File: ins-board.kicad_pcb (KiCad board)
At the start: 4 copper layers, 50 x 23 mm, 94 parts, among them P1 PWR, P2 Power (Solder Pad), Q1 FDN306P, Q2 FDC638APZ, U1 24LC128, U10 HMC5883L, U11 H3LIS331DL, U2 STM32F415RGT6, U3 LTC4412, U4 MAX3051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

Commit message: optimize routing
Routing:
- net GND: track 140.3 -> 142.7 mm, vias 25 -> 26
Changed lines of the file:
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@@
     (thickness 1.6)
     (drawings 13)
-    (tracks 1273)
+    (tracks 1281)
     (zones 0)
     (modules 94)
@@
   (segment (start 45.6646 38.5646) (end 45.6646 38.3872) (width 0.2032) (layer F.Cu) (net 28))
   (segment (start 45.6646 38.3872) (end 45.6646 38.5646) (width 0.2032) (layer F.Cu) (net 28))
-  (segment (start 44.4146 38.3872) (end 44.4146 38.7554) (width 0.2032) (layer F.Cu) (net 29) (status C00000))
-  (segment (start 43.4132 38.4868) (end 44.2698 38.4868) (width 0.2032) (layer B.Cu) (net 29) (status 800000))
+  (segment (start 44.4146 38.3872) (end 44.4146 38.7554) (width 0.2032) (layer F.Cu) (net 29))
+  (segment (start 43.4132 38.4868) (end 44.2698 38.4868) (width 0.2032) (layer B.Cu) (net 29))
   (segment (start 42.38 39.52) (end 43.4132 38.4868) (width 0.2032) (layer B.Cu) (net 29))
   (via (at 42.38 39.52) (size 0.706) (layers F.Cu B.Cu) (net 29))
   (segment (start 42.43 39.47) (end 42.38 39.52) (width 0.2032) (layer F.Cu) (net 29))
   (segment (start 43.7 39.47) (end 42.43 39.47) (width 0.2032) (layer F.Cu) (net 29))
-  (segment (start 44.4146 38.7554) (end 43.7 39.47) (width 0.2032) (layer F.Cu) (net 29) (status 400000))
+  (segment (start 44.4146 38.7554) (end 43.7 39.47) (width 0.2032) (layer F.Cu) (net 29))
   (segment (start 46.6 41.9) (end 46.6 42.05) (width 0.2032) (layer B.Cu) (net 29))
   (segment (start 46.6 42.05) (end 45.7 42.95) (width 0.2032) (layer B.Cu) (net 29))
@@
   (segment (start 61.4 44.4) (end 59.8 46) (width 0.2032) (layer F.Cu) (net 35))
   (segment (start 48.5 45.5) (end 49.275 45.5) (width 0.2032) (layer F.Cu) (net 35))
-  (segment (start 46.95 44.05) (end 47.04 44.05) (width 0.254) (layer F.Cu) (net 36) (status C00000))
+  (segment (start 46.95 44.05) (end 47.04 44.05) (width 0.254) (layer F.Cu) (net 36))
   (segment (start 47.62 42.23) (end 48.5 41.35) (width 0.254) (layer F.Cu) (net 36))
   (segment (start 47.62 43.47) (end 47.62 42.23) (width 0.254) (layer F.Cu) (net 36))
-  (segment (start 47.04 44.05) (end 47.62 43.47) (width 0.254) (layer F.Cu) (net 36) (status 400000))
+  (segment (start 47.04 44.05) (end 47.62 43.47) (width 0.254) (layer F.Cu) (net 36))
   (segment (start 46.75 34.2) (end 46.75 35.05) (width 0.2032) (layer F.Cu) (net 36))
   (segment (start 46.75 35.05) (end 48 36.3) (width 0.2032) (layer F.Cu) (net 36))
@@
   (segment (start 66.25 38.75) (end 66 39) (width 0.2032) (layer F.Cu) (net 51))
   (segment (start 66.25 38.75) (end 66 39) (width 0.2032) (layer F.Cu) (net 51))
+  (segment (start 39.925 36.375) (end 39.925 37.325) (width 0.254) (layer F.Cu) (net 52) (status 400000))
+  (segment (start 39.9288 37.9988) (end 39.9288 38.4868) (width 0.254) (layer B.Cu) (net 52) (status 800000))
+  (segment (start 39.59 37.66) (end 39.9288 37.9988) (width 0.254) (layer B.Cu) (net 52))
+  (via (at 39.59 37.66) (size 0.706) (layers F.Cu B.Cu) (net 52))
+  (segment (start 39.925 37.325) (end 39.59 37.66) (width 0.254) (layer F.Cu) (net 52))
   (segment (start 49.99 42.08) (end 49.99 41.91) (width 0.254) (layer F.Cu) (net 52))
-  (segment (start 49.99 41.91) (end 50.65 41.25) (width 0.254) (layer F.Cu) (net 52) (status 800000))
-  (segment (start 47.9 43.65) (end 47.9 43.5) (width 0.254) (layer B.Cu) (net 52) (status C00000))
+  (segment (start 49.99 41.91) (end 50.65 41.25) (width 0.254) (layer F.Cu) (net 52))
+  (segment (start 47.9 43.65) (end 47.9 43.5) (width 0.254) (layer B.Cu) (net 52))
   (segment (start 48.91 42.08) (end 49.99 42.08) (width 0.254) (layer F.Cu) (net 52))
   (segment (start 49.99 42.08) (end 50 42.08) (width 0.254) (layer F.Cu) (net 52))
@@
   (segment (start 48.32 43.08) (end 48.32 42.67) (width 0.254) (layer F.Cu) (net 52))
   (via (at 48.32 43.08) (size 0.706) (layers F.Cu B.Cu) (net 52))
-  (segment (start 47.9 43.5) (end 48.32 43.08) (width 0.254) (layer B.Cu) (net 52) (status 400000))
+  (segment (start 47.9 43.5) (end 48.32 43.08) (width 0.254) (layer B.Cu) (net 52))
   (segment (start 57.225 37.25) (end 55.78 37.25) (width 0.2032) (layer B.Cu) (net 52))
   (segment (start 55.6 37.07) (end 55.6 36.25) (width 0.2032) (layer B.Cu) (net 52))
@@
   (via (at 54.6 44.35) (size 0.706) (layers F.Cu B.Cu) (net 76))
   (segment (start 54.45 44.5) (end 54.6 44.35) (width 0.2032) (layer F.Cu) (net 76))
-  (segment (start 41.45 39.8) (end 41.45 33) (width 0.2032) (layer Inner2.Cu) (net 77))
-  (segment (start 41.45 33) (end 42.01 32.44) (width 0.2032) (layer Inner2.Cu) (net 77))
+  (segment (start 41.45 39.8) (end 41.45 39.25) (width 0.2032) (layer Inner2.Cu) (net 77))
+  (segment (start 42.55 38.15) (end 42.55 31.9) (width 0.2032) (layer Inner2.Cu) (net 77))
+  (segment (start 41.45 39.25) (end 42.55 38.15) (width 0.2032) (layer Inner2.Cu) (net 77))
+  (segment (start 40.73 37.75) (end 40.71 37.75) (width 0.2032) (layer B.Cu) (net 77))
+  (segment (start 39.71 36.75) (end 39 36.75) (width 0.2032) (layer B.Cu) (net 77))
+  (segment (start 40.71 37.75) (end 39.71 36.75) (width 0.2032) (layer B.Cu) (net 77))
   (segment (start 52.4 30.7) (end 53.75 30.7) (width 0.2032) (layer B.Cu) (net 77))
   (segment (start 53.75 30.7) (end 54.4 30.7) (width 0.254) (layer B.Cu) (net 77))
@@
   (via (at 41.45 39.8) (size 0.706) (layers F.Cu B.Cu) (net 77))
   (segment (start 39 36.75) (end 38.1 36.75) (width 0.2032) (layer B.Cu) (net 77))
-  (segment (start 40 37.75) (end 39 36.75) (width 0.2032) (layer B.Cu) (net 77))
-  (segment (start 40.95 37.75) (end 40 37.75) (width 0.2032) (layer B.Cu) (net 77))
+  (segment (start 40.95 37.75) (end 40.73 37.75) (width 0.2032) (layer B.Cu) (net 77))
   (segment (start 41.45 38.25) (end 40.95 37.75) (width 0.2032) (layer B.Cu) (net 77))
   (segment (start 74.25 35.9) (end 75.1 35.9) (width 0.254) (layer F.Cu) (net 77))
@@
   (segment (start 53.4 29.5) (end 54.05 28.85) (width 0.2032) (layer Inner2.Cu) (net 77))
   (segment (start 44.95 29.5) (end 53.4 29.5) (width 0.2032) (layer Inner2.Cu) (net 77))
-  (segment (start 42.01 32.44) (end 44.95 29.5) (width 0.2032) (layer Inner2.Cu) (net 77))
+  (segment (start 42.55 31.9) (end 44.95 29.5) (width 0.2032) (layer Inner2.Cu) (net 77))
   (segment (start 52.8828 28.1328) (end 54.3276 28.1328) (width 0.3556) (layer B.Cu) (net 77))
   (segment (start 54.3276 28.1328) (end 54.7116 27.7488) (width 0.3556) (layer B.Cu) (net 77))

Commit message: optimize zones
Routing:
- net GND: track 142.7 -> 143.3 mm
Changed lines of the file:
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@@
     (thickness 1.6)
     (drawings 13)
-    (tracks 1281)
+    (tracks 1282)
     (zones 0)
     (modules 94)
@@
     (22 B.Mask user)
     (23 F.Mask user)
-    (24 Dwgs.User user)
+    (24 Dwgs.User user hide)
     (25 Cmts.User user hide)
     (26 Eco1.User user)
@@
   (segment (start 66.25 38.75) (end 66 39) (width 0.2032) (layer F.Cu) (net 51))
   (segment (start 66.25 38.75) (end 66 39) (width 0.2032) (layer F.Cu) (net 51))
-  (segment (start 39.925 36.375) (end 39.925 37.325) (width 0.254) (layer F.Cu) (net 52) (status 400000))
-  (segment (start 39.9288 37.9988) (end 39.9288 38.4868) (width 0.254) (layer B.Cu) (net 52) (status 800000))
+  (segment (start 79 43.25) (end 79.65 43.25) (width 0.508) (layer Inner2.Cu) (net 52))
+  (segment (start 46.15 31.9) (end 47.6 31.9) (width 0.2032) (layer F.Cu) (net 52))
+  (via (at 48 32.3) (size 0.706) (layers F.Cu B.Cu) (net 52))
+  (segment (start 47.6 31.9) (end 48 32.3) (width 0.2032) (layer F.Cu) (net 52))
+  (segment (start 39.925 36.375) (end 39.925 37.325) (width 0.254) (layer F.Cu) (net 52))
+  (segment (start 39.9288 37.9988) (end 39.9288 38.4868) (width 0.254) (layer B.Cu) (net 52))
   (segment (start 39.59 37.66) (end 39.9288 37.9988) (width 0.254) (layer B.Cu) (net 52))
   (via (at 39.59 37.66) (size 0.706) (layers F.Cu B.Cu) (net 52))
@@
   (segment (start 44.1 43.55) (end 44.1 43.2) (width 0.2032) (layer F.Cu) (net 52))
   (via (at 44.1 43.2) (size 0.706) (layers F.Cu B.Cu) (net 52))
-  (segment (start 46.15 31.9) (end 47.6 31.9) (width 0.2032) (layer F.Cu) (net 52))
-  (via (at 48 32.3) (size 0.706) (layers F.Cu B.Cu) (net 52))
-  (segment (start 47.6 31.9) (end 48 32.3) (width 0.2032) (layer F.Cu) (net 52))
   (segment (start 57.35 27.5) (end 56.75 26.9) (width 0.3048) (layer B.Cu) (net 52))
   (segment (start 56.75 26.9) (end 56 26.9) (width 0.3048) (layer B.Cu) (net 52))
@@
   (via (at 54.6 44.35) (size 0.706) (layers F.Cu B.Cu) (net 76))
   (segment (start 54.45 44.5) (end 54.6 44.35) (width 0.2032) (layer F.Cu) (net 76))
+  (segment (start 44.275 30.175) (end 45.6 28.85) (width 0.2032) (layer Inner2.Cu) (net 77))
+  (segment (start 45.6 28.85) (end 54.05 28.85) (width 0.2032) (layer Inner2.Cu) (net 77))
   (segment (start 41.45 39.8) (end 41.45 39.25) (width 0.2032) (layer Inner2.Cu) (net 77))
   (segment (start 42.55 38.15) (end 42.55 31.9) (width 0.2032) (layer Inner2.Cu) (net 77))
@@
   (segment (start 54.95 28.85) (end 56.05 29.95) (width 0.2032) (layer Inner2.Cu) (net 77))
   (segment (start 54.05 28.85) (end 54.95 28.85) (width 0.2032) (layer Inner2.Cu) (net 77))
-  (segment (start 53.4 29.5) (end 54.05 28.85) (width 0.2032) (layer Inner2.Cu) (net 77))
-  (segment (start 44.95 29.5) (end 53.4 29.5) (width 0.2032) (layer Inner2.Cu) (net 77))
-  (segment (start 42.55 31.9) (end 44.95 29.5) (width 0.2032) (layer Inner2.Cu) (net 77))
+  (segment (start 42.55 31.9) (end 44.275 30.175) (width 0.2032) (layer Inner2.Cu) (net 77))
   (segment (start 52.8828 28.1328) (end 54.3276 28.1328) (width 0.3556) (layer B.Cu) (net 77))
   (segment (start 54.3276 28.1328) (end 54.7116 27.7488) (width 0.3556) (layer B.Cu) (net 77))
@@
     (polygon
       (pts
-        (xy 55 47.8) (xy 43 47.8) (xy 43 33) (xy 55 33)
+        (xy 55 47.8) (xy 43 47.8) (xy 42.99 32.68) (xy 44.68 30.95) (xy 49.1 30.98)
+        (xy 51.14 33.01) (xy 55 33)
       )
     )
@@
     (polygon
       (pts
-        (xy 55.8 47.8) (xy 79 47.8) (xy 79 27.2) (xy 52 27.2) (xy 52 32.4)
-        (xy 55.8 32.4)
+        (xy 55.8 48.7) (xy 78.9 48.7) (xy 78.9 33.25) (xy 77.3 31.65) (xy 72.4 31.5)
+        (xy 68.7 27.95) (xy 45.78 27.9) (xy 44.42 29.27) (xy 44.42 30.62) (xy 49.29 30.63)
+        (xy 51.1 32.4) (xy 55.8 32.4)
       )
     )
@@
     (polygon
       (pts
-        (xy 32.3 26.3) (xy 51.3 26.3) (xy 51.3 32.4) (xy 42.5 32.4) (xy 42.5 48.7)
-        (xy 32.3 48.7)
+        (xy 81.7 48.7) (xy 79.35 48.7) (xy 79.35 32.7) (xy 77.5 31.1) (xy 72.55 31.1)
+        (xy 68.9 27.5) (xy 62.45 27.5) (xy 62.05 26.92) (xy 45.75 26.9) (xy 44.11 28.64)
+        (xy 44.09 30.92) (xy 42.49 32.66) (xy 42.5 48.7) (xy 32.3 48.7) (xy 32.3 26.3)
+        (xy 81.7 26.3)
       )
     )

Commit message: optimize routing
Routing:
- net GND: track 143.3 -> 144.7 mm
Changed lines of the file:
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@@
     (thickness 1.6)
     (drawings 13)
-    (tracks 1282)
+    (tracks 1293)
     (zones 0)
     (modules 94)
@@
   )
   (setup
-    (last_trace_width 0.2032)
+    (last_trace_width 0.254)
     (user_trace_width 0.1524)
     (user_trace_width 0.2032)
@@
   (segment (start 61.05 43.85) (end 56.15 43.85) (width 0.2032) (layer B.Cu) (net 27))
   (segment (start 62.2 42.7) (end 61.05 43.85) (width 0.2032) (layer B.Cu) (net 27))
-  (segment (start 45.6646 38.3872) (end 45.6646 38.9646) (width 0.2032) (layer F.Cu) (net 28))
-  (segment (start 45.6646 38.9646) (end 46.2 39.5) (width 0.2032) (layer F.Cu) (net 28))
+  (segment (start 45.6646 38.3872) (end 45.8 38.5226) (width 0.2032) (layer F.Cu) (net 28))
+  (segment (start 45.8 38.5226) (end 45.8 39.1) (width 0.2032) (layer F.Cu) (net 28))
+  (segment (start 45.8 39.1) (end 46.2 39.5) (width 0.2032) (layer F.Cu) (net 28))
   (segment (start 46.85 39.75) (end 46.45 39.75) (width 0.2032) (layer F.Cu) (net 28))
   (segment (start 46.45 39.75) (end 46.2 39.5) (width 0.2032) (layer F.Cu) (net 28))
@@
   (segment (start 66.25 38.75) (end 66 39) (width 0.2032) (layer F.Cu) (net 51))
   (segment (start 66.25 38.75) (end 66 39) (width 0.2032) (layer F.Cu) (net 51))
+  (segment (start 60.6 33) (end 60.45 33.15) (width 0.254) (layer F.Cu) (net 52))
+  (segment (start 59.5 33.15) (end 59.2 33.45) (width 0.254) (layer F.Cu) (net 52) (status C00000))
+  (segment (start 59.7 33.15) (end 59.5 33.15) (width 0.254) (layer F.Cu) (net 52) (status C00000))
+  (segment (start 60.45 33.15) (end 59.7 33.15) (width 0.254) (layer F.Cu) (net 52) (status 800000))
+  (segment (start 60.6 32.45) (end 60.25 32.8) (width 0.254) (layer F.Cu) (net 52) (status 400000))
+  (segment (start 60.25 32.8) (end 60.25 33) (width 0.254) (layer F.Cu) (net 52))
+  (segment (start 60.25 33) (end 60.6 33) (width 0.254) (layer F.Cu) (net 52))
+  (segment (start 50.65 41.25) (end 50.65 41.42) (width 0.254) (layer F.Cu) (net 52) (status C00000))
+  (segment (start 50.65 41.42) (end 49.99 42.08) (width 0.254) (layer F.Cu) (net 52) (status 400000))
+  (segment (start 43.2428 40.386) (end 43.2428 40.6072) (width 0.254) (layer F.Cu) (net 52))
+  (segment (start 42.6 41.25) (end 42.4 41.25) (width 0.254) (layer F.Cu) (net 52))
+  (segment (start 43.2428 40.6072) (end 42.6 41.25) (width 0.254) (layer F.Cu) (net 52))
+  (segment (start 43.5984 34.544) (end 43.5984 34.8016) (width 0.254) (layer F.Cu) (net 52))
+  (segment (start 43.5984 34.8016) (end 43.1646 35.2354) (width 0.254) (layer F.Cu) (net 52))
   (segment (start 79 43.25) (end 79.65 43.25) (width 0.508) (layer Inner2.Cu) (net 52))
   (segment (start 46.15 31.9) (end 47.6 31.9) (width 0.2032) (layer F.Cu) (net 52))
@@
   (via (at 39.59 37.66) (size 0.706) (layers F.Cu B.Cu) (net 52))
   (segment (start 39.925 37.325) (end 39.59 37.66) (width 0.254) (layer F.Cu) (net 52))
-  (segment (start 49.99 42.08) (end 49.99 41.91) (width 0.254) (layer F.Cu) (net 52))
-  (segment (start 49.99 41.91) (end 50.65 41.25) (width 0.254) (layer F.Cu) (net 52))
   (segment (start 47.9 43.65) (end 47.9 43.5) (width 0.254) (layer B.Cu) (net 52))
   (segment (start 48.91 42.08) (end 49.99 42.08) (width 0.254) (layer F.Cu) (net 52))
@@
   (segment (start 50 42.75) (end 50 42.08) (width 0.2032) (layer F.Cu) (net 52))
   (segment (start 47.9 39.55) (end 49.4 39.55) (width 0.254) (layer B.Cu) (net 52))
-  (segment (start 43.2428 40.386) (end 43.2428 40.4072) (width 0.254) (layer F.Cu) (net 52))
-  (segment (start 43.2428 40.4072) (end 42.4 41.25) (width 0.254) (layer F.Cu) (net 52))
   (segment (start 42.4 41.25) (end 42.65 41.25) (width 0.2032) (layer B.Cu) (net 52))
   (via (at 42.4 41.25) (size 0.706) (layers F.Cu B.Cu) (net 52))
@@
   (segment (start 42.95 40.3) (end 43.4632 39.7868) (width 0.254) (layer B.Cu) (net 52))
   (segment (start 41.9146 38.3872) (end 41.9146 36.1872) (width 0.254) (layer F.Cu) (net 52))
-  (segment (start 43.1646 36.1872) (end 43.1646 34.9778) (width 0.254) (layer F.Cu) (net 52))
-  (segment (start 43.1646 34.9778) (end 43.5984 34.544) (width 0.254) (layer F.Cu) (net 52))
+  (segment (start 43.1646 36.1872) (end 43.1646 35.2354) (width 0.254) (layer F.Cu) (net 52))
   (segment (start 66.7 41.975) (end 66.7 40.65) (width 0.2032) (layer B.Cu) (net 52))
   (via (at 66.7 40.65) (size 0.706) (layers F.Cu B.Cu) (net 52))
@@
   (via (at 55.1 40.8) (size 0.706) (layers F.Cu B.Cu) (net 52))
   (segment (start 61 30.4) (end 61 32.6) (width 0.254) (layer B.Cu) (net 52))
+  (segment (start 61 32.6) (end 60.6 33) (width 0.254) (layer B.Cu) (net 52))
   (via (at 60.6 33) (size 0.706) (layers F.Cu B.Cu) (net 52))
   (segment (start 60.6 33) (end 60.6 32.45) (width 0.254) (layer F.Cu) (net 52))
-  (segment (start 61 32.6) (end 60.6 33) (width 0.254) (layer B.Cu) (net 52))
   (segment (start 66.25 45.2) (end 67.6 45.2) (width 0.254) (layer B.Cu) (net 52))
   (segment (start 67.6 45.2) (end 67.7 45.1) (width 0.254) (layer B.Cu) (net 52))
@@
   (segment (start 61.6 32.6) (end 61.45 32.45) (width 0.254) (layer F.Cu) (net 52))
   (segment (start 61.45 32.45) (end 60.2 32.45) (width 0.254) (layer F.Cu) (net 52))
-  (segment (start 60.2 32.45) (end 59.2 33.45) (width 0.3048) (layer F.Cu) (net 52))
   (segment (start 77.35 31.125) (end 78.375 31.125) (width 0.3048) (layer F.Cu) (net 52))
   (segment (start 78.375 32.375) (end 77.35 32.375) (width 0.3048) (layer B.Cu) (net 52))
@@
   (via (at 54.6 44.35) (size 0.706) (layers F.Cu B.Cu) (net 76))
   (segment (start 54.45 44.5) (end 54.6 44.35) (width 0.2032) (layer F.Cu) (net 76))
+  (segment (start 70.35 31.65) (end 70.45 31.65) (width 0.2032) (layer F.Cu) (net 77) (status C00000))
+  (segment (start 70.95 32.15) (end 70.95 32.35) (width 0.2032) (layer F.Cu) (net 77))
+  (segment (start 70.45 31.65) (end 70.95 32.15) (width 0.2032) (layer F.Cu) (net 77) (status 400000))
   (segment (start 44.275 30.175) (end 45.6 28.85) (width 0.2032) (layer Inner2.Cu) (net 77))
   (segment (start 45.6 28.85) (end 54.05 28.85) (width 0.2032) (layer Inner2.Cu) (net 77))
@@
   (segment (start 63.44 46.99) (end 63.8 47.35) (width 0.254) (layer F.Cu) (net 77))
   (segment (start 63.1324 46.99) (end 63.44 46.99) (width 0.254) (layer F.Cu) (net 77))
-  (segment (start 70.35 31.65) (end 70.35 31.75) (width 0.2032) (layer F.Cu) (net 77))
   (segment (start 72.45 32.7) (end 73.3 31.85) (width 0.2032) (layer F.Cu) (net 77))
   (segment (start 71.3 32.7) (end 72.45 32.7) (width 0.2032) (layer F.Cu) (net 77))
-  (segment (start 70.35 31.75) (end 71.3 32.7) (width 0.2032) (layer F.Cu) (net 77))
+  (segment (start 70.95 32.35) (end 71.3 32.7) (width 0.2032) (layer F.Cu) (net 77))
   (segment (start 69.25 45.5) (end 69.65 45.5) (width 0.254) (layer F.Cu) (net 77))
   (segment (start 69.7 45.5) (end 70.5 46.3) (width 0.254) (layer F.Cu) (net 77))

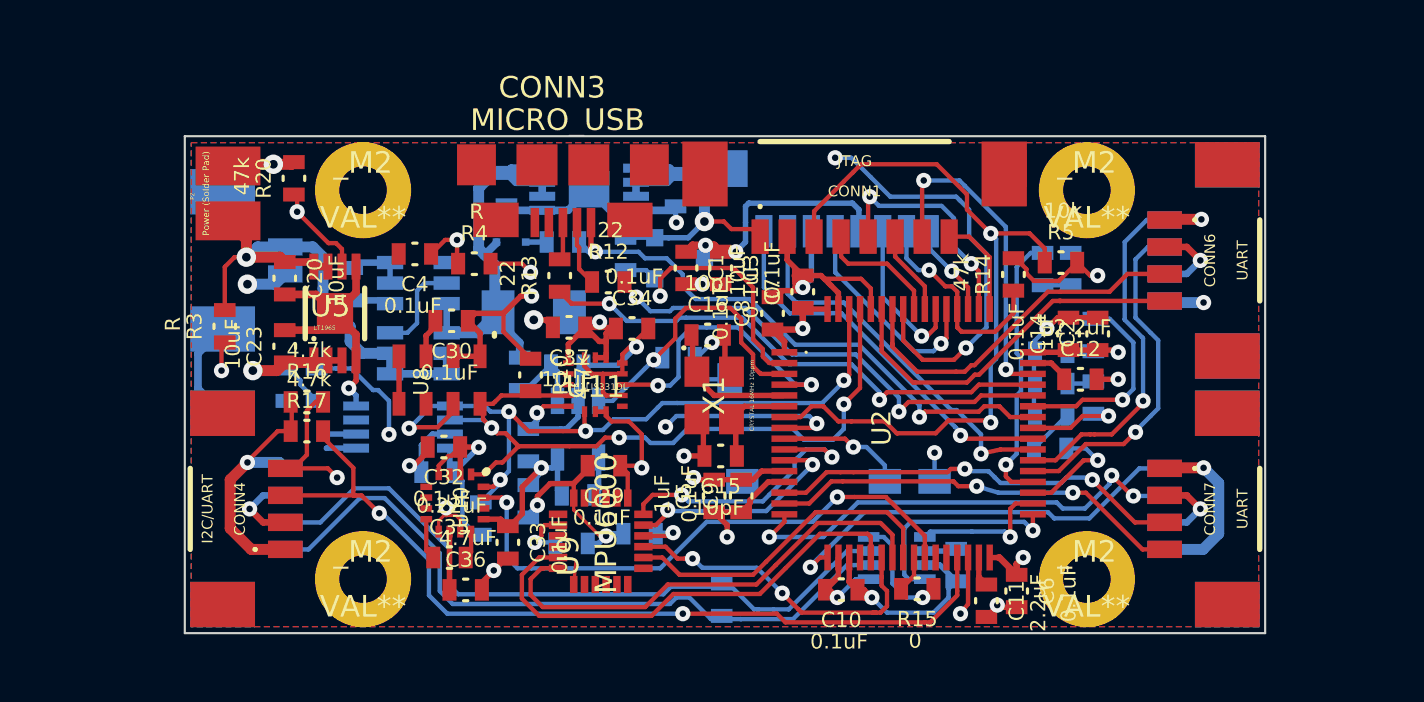
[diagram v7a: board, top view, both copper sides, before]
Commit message: replaced silkscreen with simple connector labels
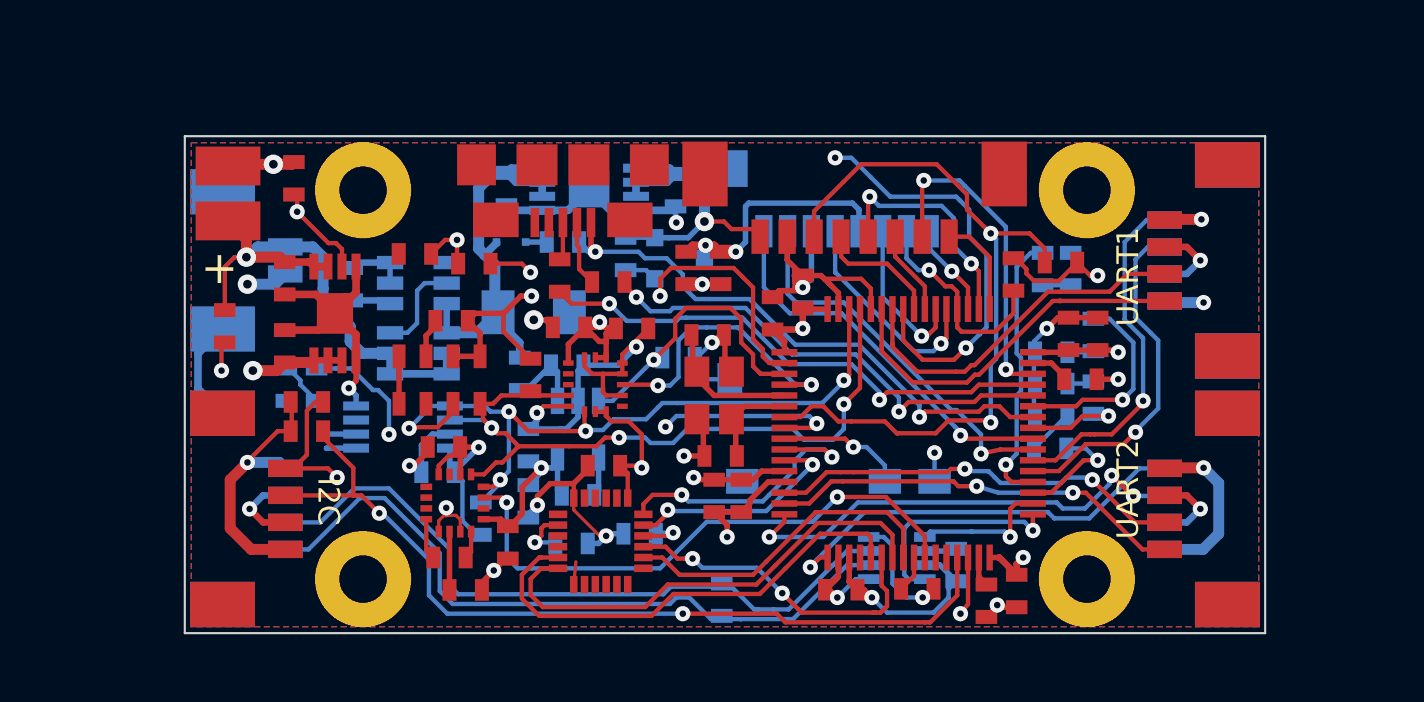
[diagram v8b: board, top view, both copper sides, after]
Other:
- board text added: "+"
- board text added: "CAN"
- board text added: "I2C"
- board text added: "PWR"
- board text added: "UART1"
- board text added: "UART2"
- board text added: "UART3"
- board text added: "UART4"
